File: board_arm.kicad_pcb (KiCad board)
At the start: 2 copper layers, 314.3 x 95.2 mm, 158 parts, among them SW1 SW_SPDT, U1 STM32F072CBT6, U2 PRTR5V0U2X, U3 MCP1725-3302E_SN

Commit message: Adjust board measurements and position, add extra holes, move some traces to fit, reverse space stab holes
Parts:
- K_SPACE1: footprint MX_Alps_Hybrid:MXOnly-6.25U-NoLED -> MX_Alps_Hybrid:MXOnly-6.25U-ReversedStabilizers-NoLED
- moved D39 5.09 mm to (231.5, 106.0), turned to 180 degrees
- moved D35 5.09 mm to (155.3, 106.0), turned to 180 degrees
- moved USB1 1.23 mm to (338.9, 61.0)
- moved C7 1.23 mm to (336.1, 72.2)
- moved C8 1.23 mm to (338.6, 82.9)
- moved C9 1.23 mm to (338.6, 80.8)
- moved R2 1.23 mm to (335.0, 77.2)
- moved R4 1.23 mm to (337.2, 69.1)
- moved R5 1.23 mm to (340.6, 69.1)
- moved U2 1.23 mm to (339.1, 72.6)
- moved U3 1.23 mm to (339.9, 77.3)
- moved SW1 0.81 mm to (353.9, 108.8)
- moved D15 0.70 mm to (359.7, 73.0)
- moved D66 0.70 mm to (359.7, 149.2)
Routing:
- net ROW2: track 316.0 -> 332.8 mm
- net COL13: track 125.0 -> 119.7 mm
- net GND: track 171.4 -> 166.7 mm
- net Net-(D39-Pad2): track 6.82 -> 3.49 mm
- net Net-(D35-Pad2): track 6.82 -> 3.49 mm
- net Net-(R1-Pad2): track 24.8 -> 25.6 mm
- net ROW4: track 329.0 -> 328.3 mm
- net ROW0: track 375.4 -> 374.7 mm
- net Net-(D66-Pad2): track 6.82 -> 6.12 mm
- net Net-(D15-Pad2): track 6.82 -> 6.12 mm
- net D-: track 67.4 -> 68.0 mm
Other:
- board size 314.3 x 95.2 mm -> 314.8 x 96.2 mm

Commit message: decalage à gauche du MCU de 20 mil et reroutage
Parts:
- moved D30 10.5 mm to (358.6, 102.5)
- moved 3V3 1.83 mm to (345.4, 122.9)
- moved C1 1.83 mm to (357.2, 135.0)
- moved C2 1.83 mm to (347.5, 132.2)
- moved C4 1.83 mm to (349.4, 127.0)
- moved GND 1.83 mm to (345.4, 119.9)
- moved LED1 1.83 mm to (351.5, 123.0)
- moved NR 1.83 mm to (350.0, 137.2)
- moved R1 1.83 mm to (342.9, 122.4)
- moved R10 1.83 mm to (350.0, 118.4)
- moved R3 1.83 mm to (357.2, 126.0)
- moved SWDC 1.83 mm to (343.9, 127.0)
- moved SWDD 1.83 mm to (348.5, 122.9)
- moved C3 1.83 mm to (354.2, 128.6)
- moved C6 1.83 mm to (352.3, 133.8)
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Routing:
- net GND: track 166.7 -> 154.5 mm, vias 17 -> 18
- net Net-(D30-Pad2): track 7.31 -> 16.4 mm
- net ROW1: track 351.9 -> 343.3 mm
- net COL3: track 316.1 -> 323.6 mm
- net COL5: track 286.3 -> 292.5 mm
- net COL4: track 303.6 -> 309.3 mm
- net COL6: track 291.0 -> 295.5 mm
- net COL1: track 376.6 -> 379.2 mm
- net COL8: track 242.0 -> 239.5 mm
- net COL9: track 229.6 -> 227.1 mm
- net ROW2: track 332.8 -> 335.2 mm
- net COL2: track 359.2 -> 361.3 mm
- net Net-(R1-Pad2): track 25.6 -> 27.6 mm
- net COL0: track 397.5 -> 399.1 mm
- net PWRGD: track 79.3 -> 80.9 mm
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
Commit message: Fix pcb measurement
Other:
- board size 314.8 x 96.2 mm -> 312.3 x 96.2 mm
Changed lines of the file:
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@@
     (add_net GND)
   )
+  (module MX_Alps_Hybrid:MXOnly-1.25U-NoLED (layer F.Cu)
+    (at 59.53125 149.225)
+    (fp_text reference K_CTRL1 (at 0 3.175) (layer Dwgs.User)
+      (effects (font (size 1 1) (thickness 0.15)))
+    )
+    (fp_text value MX-1.25U (at 0 -7.9375) (layer Dwgs.User)
+      (effects (font (size 1 1) (thickness 0.15)))
+    )
+    (fp_line (start -11.90625 9.525) (end -11.90625 -9.525) (layer Dwgs.User) (width 0.15))
+    (fp_line (start -11.90625 9.525) (end 11.90625 9.525) (layer Dwgs.User) (width 0.15))
+    (fp_line (start 11.90625 -9.525) (end 11.90625 9.525) (layer Dwgs.User) (width 0.15))
+    (fp_line (start -11.90625 -9.525) (end 11.90625 -9.525) (layer Dwgs.User) (width 0.15))
+    (fp_line (start -7 -7) (end -7 -5) (layer Dwgs.User) (width 0.15))
+    (fp_line (start -5 -7) (end -7 -7) (layer Dwgs.User) (width 0.15))
+    (fp_line (start -7 7) (end -5 7) (layer Dwgs.User) (width 0.15))
+    (fp_line (start -7 5) (end -7 7) (layer Dwgs.User) (width 0.15))
+    (fp_line (start 7 7) (end 7 5) (layer Dwgs.User) (width 0.15))
+    (fp_line (start 5 7) (end 7 7) (layer Dwgs.User) (width 0.15))
+    (fp_line (start 7 -7) (end 7 -5) (layer Dwgs.User) (width 0.15))
+    (fp_line (start 5 -7) (end 7 -7) (layer Dwgs.User) (width 0.15))
+    (pad "" np_thru_hole circle (at 5.08 0 48.0996) (size 1.75 1.75) (drill 1.75) (layers *.Cu *.Mask))
+    (pad "" np_thru_hole circle (at -5.08 0 48.0996) (size 1.75 1.75) (drill 1.75) (layers *.Cu *.Mask))
+    (pad 1 thru_hole circle (at -3.81 -2.54) (size 2.25 2.25) (drill 1.47) (layers *.Cu B.Mask)
+      (net 87 COL0))
+    (pad "" np_thru_hole circle (at 0 0) (size 3.9878 3.9878) (drill 3.9878) (layers *.Cu *.Mask))
+    (pad 2 thru_hole circle (at 2.54 -5.08) (size 2.25 2.25) (drill 1.47) (layers *.Cu B.Mask)
+      (net 63 "Net-(D57-Pad2)"))
+  )
   (module MX_Alps_Hybrid:MXOnly-6.25U-ReversedStabilizers-NoLED (layer F.Cu)
     (at 173.83125 149.225)
@@
   )
   (module MX_Alps_Hybrid:MXOnly-1.25U-NoLED (layer F.Cu)
-    (at 59.53125 149.225)
-    (fp_text reference K_CTRL1 (at 0 3.175) (layer Dwgs.User)
-      (effects (font (size 1 1) (thickness 0.15)))
-    )
-    (fp_text value MX-1.25U (at 0 -7.9375) (layer Dwgs.User)
-      (effects (font (size 1 1) (thickness 0.15)))
-    )
-    (fp_line (start -11.90625 9.525) (end -11.90625 -9.525) (layer Dwgs.User) (width 0.15))
-    (fp_line (start -11.90625 9.525) (end 11.90625 9.525) (layer Dwgs.User) (width 0.15))
-    (fp_line (start 11.90625 -9.525) (end 11.90625 9.525) (layer Dwgs.User) (width 0.15))
-    (fp_line (start -11.90625 -9.525) (end 11.90625 -9.525) (layer Dwgs.User) (width 0.15))
-    (fp_line (start -7 -7) (end -7 -5) (layer Dwgs.User) (width 0.15))
-    (fp_line (start -5 -7) (end -7 -7) (layer Dwgs.User) (width 0.15))
-    (fp_line (start -7 7) (end -5 7) (layer Dwgs.User) (width 0.15))
-    (fp_line (start -7 5) (end -7 7) (layer Dwgs.User) (width 0.15))
-    (fp_line (start 7 7) (end 7 5) (layer Dwgs.User) (width 0.15))
-    (fp_line (start 5 7) (end 7 7) (layer Dwgs.User) (width 0.15))
-    (fp_line (start 7 -7) (end 7 -5) (layer Dwgs.User) (width 0.15))
-    (fp_line (start 5 -7) (end 7 -7) (layer Dwgs.User) (width 0.15))
-    (pad "" np_thru_hole circle (at 5.08 0 48.0996) (size 1.75 1.75) (drill 1.75) (layers *.Cu *.Mask))
-    (pad "" np_thru_hole circle (at -5.08 0 48.0996) (size 1.75 1.75) (drill 1.75) (layers *.Cu *.Mask))
-    (pad 1 thru_hole circle (at -3.81 -2.54) (size 2.25 2.25) (drill 1.47) (layers *.Cu B.Mask)
-      (net 87 COL0))
-    (pad "" np_thru_hole circle (at 0 0) (size 3.9878 3.9878) (drill 3.9878) (layers *.Cu *.Mask))
-    (pad 2 thru_hole circle (at 2.54 -5.08) (size 2.25 2.25) (drill 1.47) (layers *.Cu B.Mask)
-      (net 63 "Net-(D57-Pad2)"))
-  )
-  (module MX_Alps_Hybrid:MXOnly-1.25U-NoLED (layer F.Cu)
     (at 245.26875 149.225)
     (fp_text reference K_RALT1 (at 0 3.175) (layer Dwgs.User)
@@
   (gr_poly (pts (xy 347.472 127) (xy 354.076 127) (xy 354.076 133.604) (xy 347.472 133.604)) (layer F.SilkS) (width 0.15))
   (gr_circle (center 338.925 109.5375) (end 343.925 109.5375) (layer Edge.Cuts) (width 0.2))
-  (gr_line (start 356.925 158.725) (end 50.15 158.725) (layer Edge.Cuts) (width 0.2))
+  (gr_line (start 356.925 158.725) (end 52.65 158.725) (layer Edge.Cuts) (width 0.2))
   (gr_line (start 360.925 66.525) (end 360.925 154.725) (layer Edge.Cuts) (width 0.2))
-  (gr_line (start 50.15 62.525) (end 356.925 62.525) (layer Edge.Cuts) (width 0.2))
-  (gr_line (start 46.15 154.725) (end 46.15 66.525) (layer Edge.Cuts) (width 0.2))
-  (gr_arc (start 50.15 154.725) (end 46.15 154.725) (angle -90) (layer Edge.Cuts) (width 0.2))
-  (gr_arc (start 50.15 66.525) (end 50.15 62.525) (angle -90) (layer Edge.Cuts) (width 0.2))
+  (gr_line (start 52.65 62.525) (end 356.925 62.525) (layer Edge.Cuts) (width 0.2))
+  (gr_line (start 48.65 154.725) (end 48.65 66.525) (layer Edge.Cuts) (width 0.2))
+  (gr_arc (start 52.65 154.725) (end 48.65 154.725) (angle -90) (layer Edge.Cuts) (width 0.2))
+  (gr_arc (start 52.65 66.525) (end 52.65 62.525) (angle -90) (layer Edge.Cuts) (width 0.2))
   (gr_arc (start 356.925 154.725) (end 356.925 158.725) (angle -90) (layer Edge.Cuts) (width 0.2))
   (gr_arc (start 356.925 66.525) (end 360.925 66.525) (angle -90) (layer Edge.Cuts) (width 0.2))
@@
     )
   )
-  (zone (net 1) (net_name GND) (layer F.Cu) (hatch edge 0.508)
+  (zone (net 1) (net_name GND) (layer B.Cu) (hatch edge 0.508)
     (connect_pads (clearance 0.381))
     (min_thickness 0.254)
@@
     (polygon
       (pts
-        (xy 361.41025 66.00825) (xy 361.442 154.94) (xy 357.759 159.004) (xy 49.53 159.004) (xy 46.101 155.321)
-        (xy 46.228 66.04) (xy 49.53 62.484) (xy 357.886 62.484)
+        (xy 361.061 64.897) (xy 361.061 156.21) (xy 358.648 158.877) (xy 50.927 158.877) (xy 48.514 156.337)
+        (xy 48.514 65.024) (xy 50.927 62.484) (xy 358.521 62.357)
       )
     )
   )
-  (zone (net 1) (net_name GND) (layer B.Cu) (hatch edge 0.508)
+  (zone (net 1) (net_name GND) (layer F.Cu) (hatch edge 0.508)
     (connect_pads (clearance 0.381))
     (min_thickness 0.254)
@@
     (polygon
       (pts
-        (xy 361.41025 66.00825) (xy 361.442 154.94) (xy 357.759 159.004) (xy 49.53 159.004) (xy 46.101 155.321)
-        (xy 46.228 66.04) (xy 49.53 62.484) (xy 357.886 62.484)
+        (xy 361.061 64.897) (xy 361.061 156.21) (xy 358.648 158.877) (xy 50.927 158.877) (xy 48.514 156.337)
+        (xy 48.514 65.024) (xy 50.927 62.484) (xy 358.521 62.357)
       )
     )

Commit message: Add mounting holes and reroute
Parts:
- added H1: Leopold-MountingHole, locallib:Leopold-MountingHole, F.Cu at (65.2, 73.0)
- added H2: Leopold-MountingHole, locallib:Leopold-MountingHole, F.Cu at (131.8, 92.1)
- added H3: Leopold-MountingHole, locallib:Leopold-MountingHole, F.Cu at (265.2, 92.1)
- added H4: Leopold-MountingHole, locallib:Leopold-MountingHole, F.Cu at (196.8, 111.1)
- added H5: Leopold-MountingHole, locallib:Leopold-MountingHole, F.Cu at (127.1, 130.2)
- added H6: Leopold-MountingHole, locallib:Leopold-MountingHole, F.Cu at (279.8, 130.2)
- added H7: Leopold-MountingHole, locallib:Leopold-MountingHole, F.Cu at (67.5, 149.2)
- added H8: Leopold-MountingHole, locallib:Leopold-MountingHole, F.Cu at (344.4, 149.2)
- added H9: Leopold-MountingHole, locallib:Leopold-MountingHole, F.Cu at (344.4, 73.0)
- moved D54 5.09 mm to (279.8, 125.1), turned to 180 degrees
- moved D57 5.08 mm to (67.6, 144.1), turned to 180 degrees
- moved D19 5.08 mm to (131.8, 87.0), turned to 180 degrees
- moved D26 5.08 mm to (265.2, 87.0), turned to 180 degrees
- moved D1 5.08 mm to (65.2, 67.9), turned to 180 degrees
- moved D46 5.08 mm to (127.0, 125.1), turned to 180 degrees
- moved D65 0.89 mm to (340.4, 149.2)
- moved D37 0.38 mm to (193.3, 111.1)
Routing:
- net ROW3: track 302.3 -> 322.6 mm
- net ROW1: track 343.3 -> 363.4 mm
- net (no net): track 75.7 -> 86.2 mm
- net ROW4: track 327.6 -> 335.2 mm
- net ROW0: track 376.1 -> 380.4 mm
- net ROW2: track 335.2 -> 338.4 mm
- net Net-(D46-Pad2): track 6.76 -> 3.75 mm
- net Net-(D1-Pad2): track 6.82 -> 3.81 mm
- net Net-(D26-Pad2): track 6.82 -> 3.81 mm
- net Net-(D19-Pad2): track 6.82 -> 3.81 mm
- net Net-(D57-Pad2): track 6.82 -> 3.84 mm
- net Net-(D54-Pad2): track 6.82 -> 4.13 mm
- net Net-(D65-Pad2): track 6.82 -> 5.97 mm
- net COL14: track 37.5 -> 36.9 mm
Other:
- outline, holes or cut-outs redrawn

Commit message: Tweak positions according to print
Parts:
- moved D39 5.09 mm to (231.9, 111.1), turned to 90 degrees
- moved D40 5.09 mm to (250.6, 106.0), turned to 180 degrees
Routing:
- net Net-(D39-Pad2): track 3.49 -> 6.95 mm
- net Net-(D40-Pad2): track 6.82 -> 3.49 mm
- net COL0: track 399.1 -> 400.7 mm
- net Net-(D30-Pad2): track 16.4 -> 15.9 mm
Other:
- outline, holes or cut-outs redrawn

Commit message: • Route around the new holes ✔️ 	• Refill ✔️ 	• Curse at the giant rectangle no-copper zones ✔️ 	• Glace absent-mindedly at the DRC ✔️ 	• Generate Gerbers ✔️
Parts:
- moved C8 4.08 mm to (337.8, 86.9)
- moved C9 4.08 mm to (337.8, 84.8)
- moved R2 3.43 mm to (334.3, 80.5)
- moved U3 3.43 mm to (339.2, 80.6)
- moved C3 0.35 mm to (354.2, 129.0)
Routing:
- net GND: track 154.7 -> 138.3 mm, vias 18 -> 22
- net (no net): track 86.2 -> 75.7 mm, vias 0 -> 1
- net +3V3: track 120.6 -> 117.4 mm
- net +5V: track 20.8 -> 23.8 mm
- net PWRGD: track 80.9 -> 77.9 mm
- net D-: track 69.1 -> 67.0 mm
- net COL10: track 222.5 -> 221.2 mm
- net COL8: track 239.5 -> 238.4 mm
- net D+: track 67.1 -> 66.1 mm
- net COL9: track 227.1 -> 226.3 mm
- net Net-(C8-Pad1): track 6.55 -> 7.38 mm
- net COL11: track 195.5 -> 194.9 mm

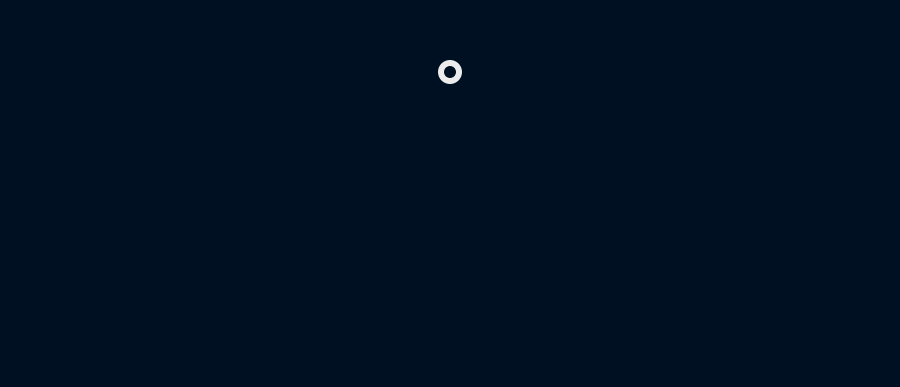
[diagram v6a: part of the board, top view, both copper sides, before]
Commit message: Remove via place outside the board
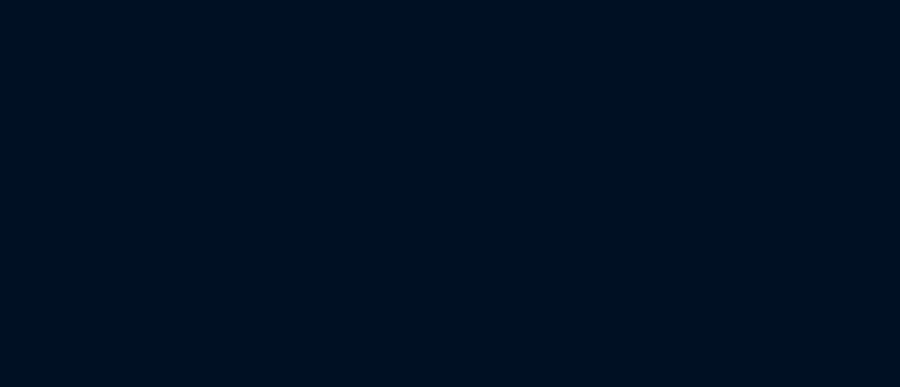
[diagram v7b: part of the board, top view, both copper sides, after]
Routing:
- net (no net): vias 1 -> 0
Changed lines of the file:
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@@
     (thickness 1.6)
     (drawings 90)
-    (tracks 1256)
+    (tracks 1255)
     (zones 0)
     (modules 167)
@@
   (segment (start 135.128 151.384) (end 155.956 151.384) (width 0.25) (layer F.Cu) (net 0))
   (segment (start 155.956 151.384) (end 155.956 135.128) (width 0.25) (layer F.Cu) (net 0))
-  (via (at 309.372 47.244) (size 0.8) (drill 0.4) (layers F.Cu B.Cu) (net 0))
   (via (at 359.156 139.7) (size 0.8) (drill 0.4) (layers F.Cu B.Cu) (net 1))
   (via (at 347.98 124.46) (size 0.8) (drill 0.4) (layers F.Cu B.Cu) (net 1))

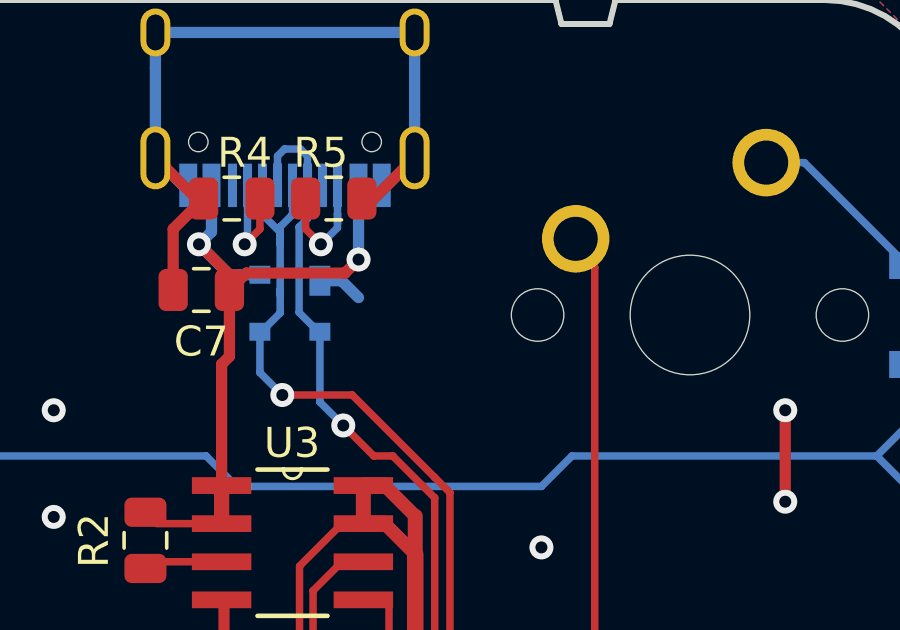
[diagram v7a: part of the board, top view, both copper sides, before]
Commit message: Make the hole next to USB into a GND pad, and regen fill zones
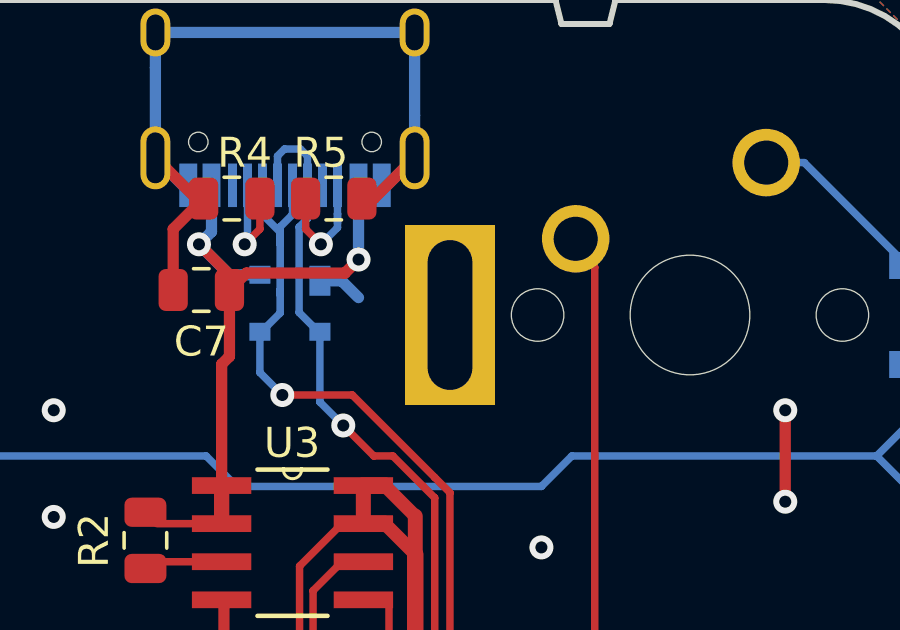
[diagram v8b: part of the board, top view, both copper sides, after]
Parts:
- H9: value Leopold-MountingHole -> Leopold-MountingPad; footprint locallib:Leopold-MountingHole -> locallib:Leopold-MountingPad
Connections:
- H9 pad : (no net) -> GND
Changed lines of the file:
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@@
-(kicad_pcb (version 20171130) (host pcbnew "(5.0.2)-1")
+(kicad_pcb (version 20171130) (host pcbnew "(5.1.0)-1")
   (general
     (thickness 1.6)
@@
     (32 B.Adhes user hide)
     (33 F.Adhes user hide)
-    (34 B.Paste user hide)
-    (35 F.Paste user hide)
+    (34 B.Paste user)
+    (35 F.Paste user)
     (36 B.SilkS user hide)
     (37 F.SilkS user)
@@
     (zone_45_only no)
     (trace_min 0.2)
-    (segment_width 0.2)
-    (edge_width 0.2)
     (via_size 0.8)
     (via_drill 0.4)
@@
     (uvia_min_size 0.2)
     (uvia_min_drill 0.1)
+    (edge_width 0.2)
+    (segment_width 0.2)
     (pcb_text_width 0.3)
     (pcb_text_size 1.5 1.5)
@@
     (mod_text_size 1 1)
     (mod_text_width 0.15)
-    (pad_size 4 7)
+    (pad_size 3 6)
     (pad_drill 1.5)
     (pad_to_mask_clearance 0)
@@
       (psa4output false)
       (plotreference true)
-      (plotvalue true)
+      (plotvalue false)
       (plotinvisibletext false)
       (padsonsilk false)
@@
     (add_net GND)
   )
-  (module locallib:Leopold-MountingHole (layer F.Cu)
+  (module locallib:Leopold-MountingPad (layer F.Cu)
     (at 344.425 73.025)
     (fp_text reference H9 (at 0 5) (layer F.SilkS) hide
       (effects (font (size 1 1) (thickness 0.15)))
     )
-    (fp_text value Leopold-MountingHole (at 0 -5) (layer F.Fab) hide
+    (fp_text value Leopold-MountingPad (at 0 -5) (layer F.Fab) hide
       (effects (font (size 1 1) (thickness 0.15)))
     )
-    (fp_line (start -2 -3.5) (end 2 -3.5) (layer Dwgs.User) (width 0.15))
-    (fp_line (start 2 -3.5) (end 2 3.5) (layer Dwgs.User) (width 0.15))
-    (fp_line (start 2 3.5) (end -2 3.5) (layer Dwgs.User) (width 0.15))
     (fp_line (start -2 3.5) (end -2 -3.5) (layer Dwgs.User) (width 0.15))
-    (pad "" np_thru_hole oval (at 0 0) (size 1.5 5) (drill oval 1.5 5) (layers *.Cu *.Mask))
+    (fp_line (start 2 3.5) (end -2 3.5) (layer Dwgs.User) (width 0.15))
+    (fp_line (start 2 -3.5) (end 2 3.5) (layer Dwgs.User) (width 0.15))
+    (fp_line (start -2 -3.5) (end 2 -3.5) (layer Dwgs.User) (width 0.15))
+    (pad "" thru_hole rect (at 0 0) (size 3 6) (drill oval 1.5 5) (layers *.Cu *.Mask)
+      (net 1 GND))
   )
   (module locallib:Leopold-MountingHole (layer F.Cu)
@@
       )
     )
-  )
-  (zone (net 0) (net_name "") (layers F&B.Cu) (hatch edge 0.508)
-    (connect_pads (clearance 0.381))
-    (min_thickness 0.254)
-    (keepout (tracks not_allowed) (vias not_allowed) (copperpour not_allowed))
-    (fill (arc_segments 16) (thermal_gap 0.508) (thermal_bridge_width 0.508))
-    (polygon
-      (pts
-        (xy 346.45 76.514101) (xy 346.45 69.514101) (xy 342.45 69.514101) (xy 342.45 76.514101)
-      )
-    )
